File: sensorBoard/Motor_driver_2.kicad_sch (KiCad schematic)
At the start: 13 parts, among them Q4 BSC440N10NS3G, Q5 BSC440N10NS3G, Q6 BSC440N10NS3G, Q7 BSC440N10NS3G, U10 4N25, U11 4N25, U6 4011, U8 4011

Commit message: added the footprints, connectors left
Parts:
- R26, R27, R28, R29: footprint (none) -> Resistor_SMD:R_0805_2012Metric
- U5: footprint (none) -> Package_TO_SOT_SMD:SC-74-6_1.55x2.9mm_P0.95mm
- U6, U8: footprint (none) -> Package_SO:SOIC-14_3.9x8.7mm_P1.27mm
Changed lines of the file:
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@@
 			)
 		)
-		(property "Footprint" ""
+		(property "Footprint" "Resistor_SMD:R_0805_2012Metric"
 			(at 227.33 115.57 0)
 			(effects
@@
 			)
 		)
-		(property "Footprint" ""
+		(property "Footprint" "Resistor_SMD:R_0805_2012Metric"
 			(at 224.79 54.61 0)
 			(effects
@@
 			)
 		)
-		(property "Footprint" ""
+		(property "Footprint" "Package_SO:SOIC-14_3.9x8.7mm_P1.27mm"
 			(at 171.45 76.2 0)
 			(effects
@@
 			)
 		)
-		(property "Footprint" ""
+		(property "Footprint" "Package_SO:SOIC-14_3.9x8.7mm_P1.27mm"
 			(at 201.93 76.2 0)
 			(effects
@@
 			)
 		)
-		(property "Footprint" ""
+		(property "Footprint" "Package_SO:SOIC-14_3.9x8.7mm_P1.27mm"
 			(at 144.78 105.41 0)
 			(effects
@@
 			)
 		)
-		(property "Footprint" ""
+		(property "Footprint" "Resistor_SMD:R_0805_2012Metric"
 			(at 200.66 102.87 0)
 			(effects
@@
 			)
 		)
-		(property "Footprint" ""
+		(property "Footprint" "Package_SO:SOIC-14_3.9x8.7mm_P1.27mm"
 			(at 170.18 139.7 0)
 			(effects
@@
 			)
 		)
-		(property "Footprint" ""
+		(property "Footprint" "Package_SO:SOIC-14_3.9x8.7mm_P1.27mm"
 			(at 52.07 161.29 0)
 			(effects
@@
 			)
 		)
-		(property "Footprint" ""
+		(property "Footprint" "Package_SO:SOIC-14_3.9x8.7mm_P1.27mm"
 			(at 143.51 78.74 0)
 			(effects
@@
 			)
 		)
-		(property "Footprint" ""
+		(property "Footprint" "Package_SO:SOIC-14_3.9x8.7mm_P1.27mm"
 			(at 207.01 139.7 0)
 			(effects
@@
 			)
 		)
-		(property "Footprint" ""
+		(property "Footprint" "Package_SO:SOIC-14_3.9x8.7mm_P1.27mm"
 			(at 171.45 46.99 0)
 			(effects
@@
 			)
 		)
-		(property "Footprint" ""
+		(property "Footprint" "Package_SO:SOIC-14_3.9x8.7mm_P1.27mm"
 			(at 170.18 107.95 0)
 			(effects
@@
 			)
 		)
-		(property "Footprint" ""
+		(property "Footprint" "Package_TO_SOT_SMD:SC-74-6_1.55x2.9mm_P0.95mm"
 			(at 57.15 39.37 0)
 			(effects
@@
 			)
 		)
-		(property "Footprint" ""
+		(property "Footprint" "Resistor_SMD:R_0805_2012Metric"
 			(at 191.77 31.75 0)
 			(effects
@@
 			)
 		)
-		(property "Footprint" ""
+		(property "Footprint" "Package_SO:SOIC-14_3.9x8.7mm_P1.27mm"
 			(at 31.75 161.29 0)
 			(effects

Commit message: started the layout
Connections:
- no-connect marks 0 -> 2
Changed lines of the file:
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@@
 		(color 0 0 0 0)
+	)
+	(no_connect
+		(at 218.44 41.91)
+	)
+	(no_connect
+		(at 222.25 102.87)
 	)
 	(wire

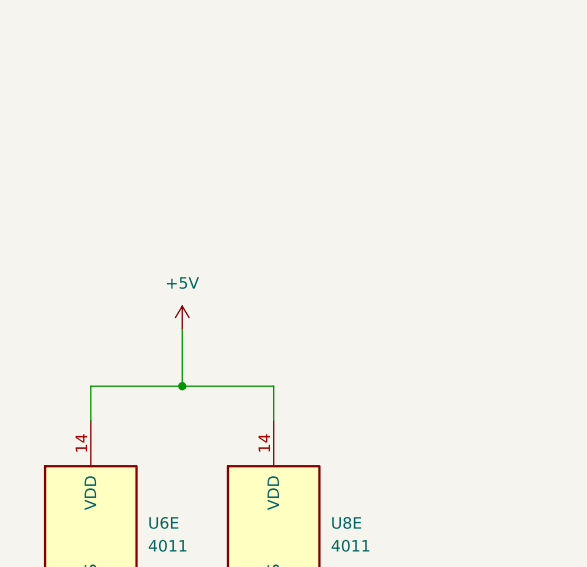
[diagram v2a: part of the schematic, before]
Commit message: started to connect layout. added 0 Ohm resistors to separate the drivers.
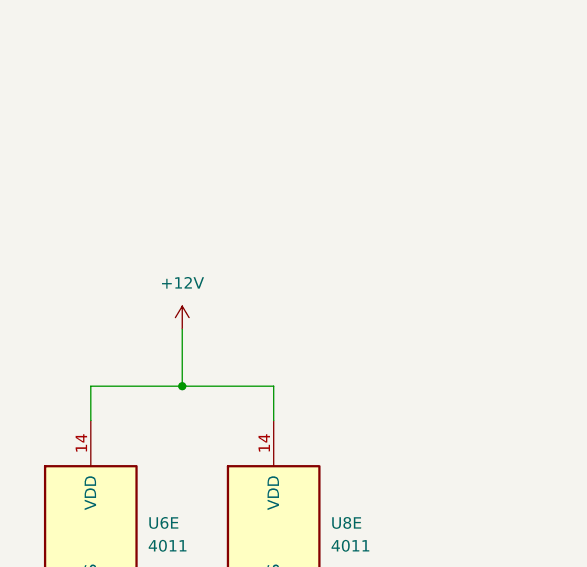
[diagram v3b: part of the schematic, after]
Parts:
- U10, U11: footprint Package_DIP:DIP-6_W7.62mm -> Package_DIP:SMDIP-6_W9.53mm_Clearance8mm
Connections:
- net +12V: now also U6.14 (VDD), U8.14 (VDD)
- net +5V: no longer U6.14 (VDD), U8.14 (VDD)
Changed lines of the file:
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@@
-	)
-	(symbol
-		(lib_id "power:+5V")
-		(at 41.91 138.43 0)
-		(unit 1)
-		(exclude_from_sim no)
-		(in_bom yes)
-		(on_board yes)
-		(dnp no)
-		(fields_autoplaced yes)
-		(property "Reference" "#PWR072"
-			(at 41.91 142.24 0)
-			(effects
-				(font
-					(size 1.27 1.27)
-				)
-				(hide yes)
-			)
-		)
-		(property "Value" "+5V"
-			(at 41.91 133.35 0)
-			(effects
-				(font
-					(size 1.27 1.27)
-				)
-			)
-		)
-		(property "Footprint" ""
-			(at 41.91 138.43 0)
-			(effects
-				(font
-					(size 1.27 1.27)
-				)
-				(hide yes)
-			)
-		)
-		(property "Datasheet" ""
-			(at 41.91 138.43 0)
-			(effects
-				(font
-					(size 1.27 1.27)
-				)
-				(hide yes)
-			)
-		)
-		(property "Description" "Power symbol creates a global label with name \"+5V\""
-			(at 41.91 138.43 0)
-			(effects
-				(font
-					(size 1.27 1.27)
-				)
-				(hide yes)
-			)
-		)
-		(pin "1"
-		)
-		(instances
-			(project "sensorBoard"
-				(path "/df1584e9-54f0-49dc-b423-5f64048efa01/9534e08a-6e1c-40ab-b25b-70f95b039843/d48dc00b-306d-4d39-acfa-cb489700cf2b"
-					(reference "#PWR072")
-					(unit 1)
-				)
-			)
-		)
 	)
 	(symbol
@@
 			)
 		)
-		(property "Footprint" "Package_DIP:DIP-6_W7.62mm"
+		(property "Footprint" "Package_DIP:SMDIP-6_W9.53mm_Clearance8mm"
 			(at 209.55 110.49 0)
 			(effects
@@
 				(path "/df1584e9-54f0-49dc-b423-5f64048efa01/9534e08a-6e1c-40ab-b25b-70f95b039843/d48dc00b-306d-4d39-acfa-cb489700cf2b"
 					(reference "U11")
+					(unit 1)
+				)
+			)
+		)
+	)
+	(symbol
+		(lib_id "power:+12V")
+		(at 41.91 138.43 0)
+		(unit 1)
+		(exclude_from_sim no)
+		(in_bom yes)
+		(on_board yes)
+		(dnp no)
+		(fields_autoplaced yes)
+		(property "Reference" "#PWR053"
+			(at 41.91 142.24 0)
+			(effects
+				(font
+					(size 1.27 1.27)
+				)
+				(hide yes)
+			)
+		)
+		(property "Value" "+12V"
+			(at 41.91 133.35 0)
+			(effects
+				(font
+					(size 1.27 1.27)
+				)
+			)
+		)
+		(property "Footprint" ""
+			(at 41.91 138.43 0)
+			(effects
+				(font
+					(size 1.27 1.27)
+				)
+				(hide yes)
+			)
+		)
+		(property "Datasheet" ""
+			(at 41.91 138.43 0)
+			(effects
+				(font
+					(size 1.27 1.27)
+				)
+				(hide yes)
+			)
+		)
+		(property "Description" "Power symbol creates a global label with name \"+12V\""
+			(at 41.91 138.43 0)
+			(effects
+				(font
+					(size 1.27 1.27)
+				)
+				(hide yes)
+			)
+		)
+		(pin "1"
+		)
+		(instances
+			(project ""
+				(path "/df1584e9-54f0-49dc-b423-5f64048efa01/9534e08a-6e1c-40ab-b25b-70f95b039843/d48dc00b-306d-4d39-acfa-cb489700cf2b"
+					(reference "#PWR053")
 					(unit 1)
 				)
@@
 			)
 		)
-		(property "Footprint" "Package_DIP:DIP-6_W7.62mm"
+		(property "Footprint" "Package_DIP:SMDIP-6_W9.53mm_Clearance8mm"
 			(at 205.74 49.53 0)
 			(effects
